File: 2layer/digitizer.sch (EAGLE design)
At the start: 56 parts, among them IC1 FT601QQFN76, X1 SMA-142-0711-881/886, X2 SMA-142-0711-881/886

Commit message: almost done allocating wires
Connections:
- net ADC_OEN: now also JP4.4
- net ADC_SLP: now also JP4.3
- net BE0: now also JP3.18; no longer JP4.24
- net BE1: now also JP3.17; no longer JP4.23
- net BE2: now also JP3.20; no longer JP4.26
- net BE3: now also JP3.19; no longer JP4.25
- net GND: now also JP3.11, JP3.12, JP3.31, JP3.32, JP3.39
- net GPIO0: now also JP3.29; no longer JP3.28
- net GPIO1: now also JP3.30; no longer JP3.27
- net OEN: now also JP3.28; no longer JP3.26
- net OVFL: now also JP3.16
- net RDN: now also JP3.27; no longer JP3.25
- net RXFN: now also JP3.24
- net SAMP0: now also JP3.3
- net SAMP1: now also JP3.6
- net SAMP2: now also JP3.5
- net SAMP3: now also JP3.8
- net SAMP4: now also JP3.7
- net SAMP5: now also JP3.10
- net SAMP6: now also JP3.9
- net SAMP7: now also JP3.13
- net SAMP8: now also JP3.14
- net SAMP9: now also JP3.15
- net SAMPCLK: now also JP3.4
- net SFT_RSTN: now also JP3.40
- net SFT_WKPN: now also JP3.38
- net SIWUN: now also JP3.25; no longer JP3.23
- net TXEN: now also JP3.23
- net WRN: now also JP3.26; no longer JP3.24

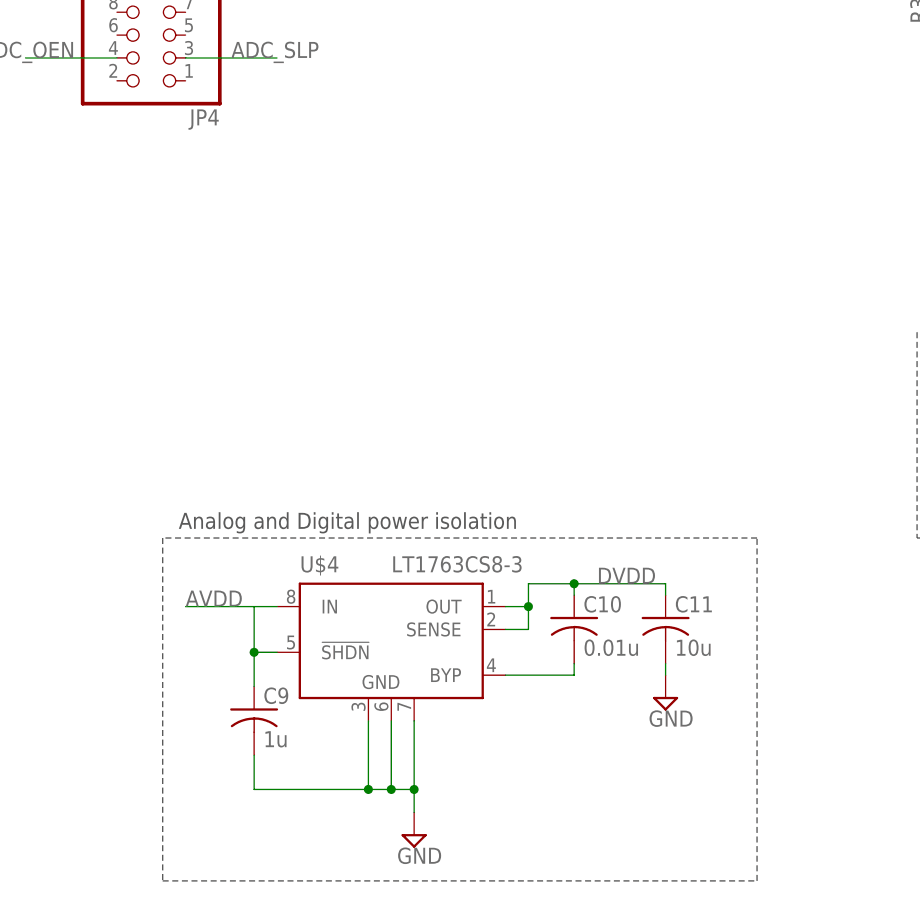
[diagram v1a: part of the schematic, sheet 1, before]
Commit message: added dual regulator solution for power isolation
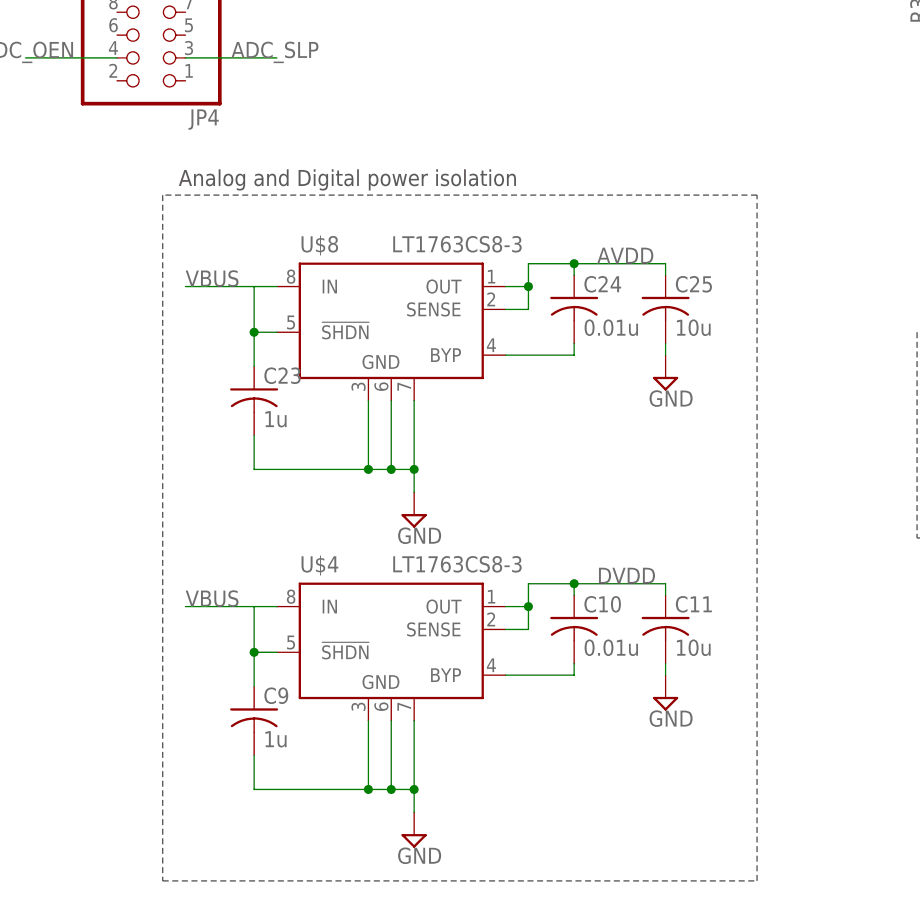
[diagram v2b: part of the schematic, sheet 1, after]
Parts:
- added C23: 1u, resistor:C-USC0402
- added C24: 0.01u, resistor:C-USC0402
- added C25: 10u, resistor:C-USC0402
- added U$8: LT1763CS8-3, linear-technology:LT1763CS8-3
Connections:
- new net N$16: C24.2, U$8.BYP
- net AVDD: now also C24.1, C25.1, U$8.OUT, U$8.SENSE; no longer C9.1, U$4.!SHDN, U$4.IN
- net GND: now also C23.2, C25.2, U$8.GND@1, U$8.GND@2, U$8.GND@3
- net VBUS: now also C23.1, C9.1, U$4.!SHDN, U$4.IN, U$8.!SHDN, U$8.IN
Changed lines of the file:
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@@
 <part name="SUPPLY37" library="supply2" deviceset="GND" device=""/>
 <part name="SUPPLY38" library="supply2" deviceset="GND" device=""/>
+<part name="U$8" library="linear-technology" deviceset="LT1763CS8" device="" technology="-3"/>
+<part name="C23" library="resistor" deviceset="C-US" device="C0402" value="1u"/>
+<part name="C24" library="resistor" deviceset="C-US" device="C0402" value="0.01u"/>
+<part name="C25" library="resistor" deviceset="C-US" device="C0402" value="10u"/>
+<part name="SUPPLY39" library="supply2" deviceset="GND" device=""/>
+<part name="SUPPLY40" library="supply2" deviceset="GND" device=""/>
 </parts>
 <sheets>
@@
 <wire x1="88.9" y1="-33.02" x2="35.56" y2="-33.02" width="0.1524" layer="97" style="longdash"/>
 <text x="37.338" y="-32.004" size="1.778" layer="97">Mixer impedance match and image filter</text>
-<wire x1="-48.26" y1="-55.88" x2="-48.26" y2="-93.98" width="0.1524" layer="97" style="longdash"/>
+<wire x1="-48.26" y1="-17.78" x2="-48.26" y2="-93.98" width="0.1524" layer="97" style="longdash"/>
 <wire x1="-48.26" y1="-93.98" x2="17.78" y2="-93.98" width="0.1524" layer="97" style="longdash"/>
-<wire x1="17.78" y1="-93.98" x2="17.78" y2="-55.88" width="0.1524" layer="97" style="longdash"/>
-<wire x1="17.78" y1="-55.88" x2="-48.26" y2="-55.88" width="0.1524" layer="97" style="longdash"/>
-<text x="-46.482" y="-54.864" size="1.778" layer="97">Analog and Digital power isolation</text>
+<wire x1="17.78" y1="-93.98" x2="17.78" y2="-17.78" width="0.1524" layer="97" style="longdash"/>
+<wire x1="17.78" y1="-17.78" x2="-48.26" y2="-17.78" width="0.1524" layer="97" style="longdash"/>
+<text x="-46.482" y="-16.764" size="1.778" layer="97">Analog and Digital power isolation</text>
 <text x="58.42" y="99.06" size="5.08" layer="97">Mixer</text>
 <text x="50.8" y="53.34" size="5.08" layer="97">ADC</text>
@@
 <instance part="SUPPLY37" gate="GND" x="-27.94" y="86.36" rot="R90"/>
 <instance part="SUPPLY38" gate="GND" x="-25.4" y="73.66" rot="R90"/>
+<instance part="U$8" gate="G$1" x="-22.86" y="-30.48"/>
+<instance part="C23" gate="G$1" x="-38.1" y="-39.37"/>
+<instance part="C24" gate="G$1" x="-2.54" y="-29.21"/>
+<instance part="C25" gate="G$1" x="7.62" y="-29.21"/>
+<instance part="SUPPLY39" gate="GND" x="-20.32" y="-53.34"/>
+<instance part="SUPPLY40" gate="GND" x="7.62" y="-38.1"/>
 </instances>
 <busses>
@@
 <pinref part="SUPPLY34" gate="GND" pin="GND"/>
 </segment>
+<segment>
+<pinref part="SUPPLY40" gate="GND" pin="GND"/>
+<pinref part="C25" gate="G$1" pin="2"/>
+<wire x1="7.62" y1="-35.56" x2="7.62" y2="-34.29" width="0.1524" layer="91"/>
+</segment>
+<segment>
+<pinref part="C23" gate="G$1" pin="2"/>
+<wire x1="-38.1" y1="-44.45" x2="-38.1" y2="-48.26" width="0.1524" layer="91"/>
+<wire x1="-38.1" y1="-48.26" x2="-25.4" y2="-48.26" width="0.1524" layer="91"/>
+<pinref part="U$8" gate="G$1" pin="GND@1"/>
+<wire x1="-25.4" y1="-48.26" x2="-25.4" y2="-40.64" width="0.1524" layer="91"/>
+<pinref part="U$8" gate="G$1" pin="GND@2"/>
+<wire x1="-25.4" y1="-48.26" x2="-22.86" y2="-48.26" width="0.1524" layer="91"/>
+<wire x1="-22.86" y1="-48.26" x2="-22.86" y2="-40.64" width="0.1524" layer="91"/>
+<junction x="-25.4" y="-48.26"/>
+<pinref part="U$8" gate="G$1" pin="GND@3"/>
+<wire x1="-22.86" y1="-48.26" x2="-20.32" y2="-48.26" width="0.1524" layer="91"/>
+<wire x1="-20.32" y1="-48.26" x2="-20.32" y2="-40.64" width="0.1524" layer="91"/>
+<junction x="-22.86" y="-48.26"/>
+<pinref part="SUPPLY39" gate="GND" pin="GND"/>
+<wire x1="-20.32" y1="-48.26" x2="-20.32" y2="-50.8" width="0.1524" layer="91"/>
+<junction x="-20.32" y="-48.26"/>
+</segment>
 </net>
 <net name="AVDD" class="0">
@@
 </segment>
 <segment>
-<pinref part="U$4" gate="G$1" pin="IN"/>
-<wire x1="-35.56" y1="-63.5" x2="-38.1" y2="-63.5" width="0.1524" layer="91"/>
-<pinref part="C9" gate="G$1" pin="1"/>
-<wire x1="-45.72" y1="-63.5" x2="-38.1" y2="-63.5" width="0.1524" layer="91"/>
-<wire x1="-38.1" y1="-63.5" x2="-38.1" y2="-68.58" width="0.1524" layer="91"/>
-<pinref part="U$4" gate="G$1" pin="!SHDN"/>
-<wire x1="-38.1" y1="-68.58" x2="-38.1" y2="-72.39" width="0.1524" layer="91"/>
-<wire x1="-35.56" y1="-68.58" x2="-38.1" y2="-68.58" width="0.1524" layer="91"/>
-<junction x="-38.1" y="-68.58"/>
-<label x="-45.72" y="-63.5" size="1.778" layer="95"/>
-</segment>
-<segment>
 <wire x1="-76.2" y1="-73.66" x2="-81.28" y2="-73.66" width="0.1524" layer="91"/>
 <wire x1="-81.28" y1="-73.66" x2="-81.28" y2="-71.12" width="0.1524" layer="91"/>
@@
 <wire x1="-104.14" y1="-73.66" x2="-104.14" y2="-71.12" width="0.1524" layer="91"/>
 <pinref part="R12" gate="G$1" pin="1"/>
+</segment>
+<segment>
+<pinref part="U$8" gate="G$1" pin="SENSE"/>
+<wire x1="-10.16" y1="-30.48" x2="-7.62" y2="-30.48" width="0.1524" layer="91"/>
+<wire x1="-7.62" y1="-30.48" x2="-7.62" y2="-27.94" width="0.1524" layer="91"/>
+<pinref part="U$8" gate="G$1" pin="OUT"/>
+<wire x1="-7.62" y1="-27.94" x2="-10.16" y2="-27.94" width="0.1524" layer="91"/>
+<wire x1="-7.62" y1="-27.94" x2="-7.62" y2="-25.4" width="0.1524" layer="91"/>
+<junction x="-7.62" y="-27.94"/>
+<pinref part="C25" gate="G$1" pin="1"/>
+<wire x1="-7.62" y1="-25.4" x2="-2.54" y2="-25.4" width="0.1524" layer="91"/>
+<wire x1="-2.54" y1="-25.4" x2="7.62" y2="-25.4" width="0.1524" layer="91"/>
+<wire x1="7.62" y1="-25.4" x2="7.62" y2="-26.67" width="0.1524" layer="91"/>
+<pinref part="C24" gate="G$1" pin="1"/>
+<wire x1="-2.54" y1="-26.67" x2="-2.54" y2="-25.4" width="0.1524" layer="91"/>
+<junction x="-2.54" y="-25.4"/>
+<label x="0" y="-25.4" size="1.778" layer="95"/>
 </segment>
 </net>
@@
 </segment>
 </net>
+<net name="N$16" class="0">
+<segment>
+<pinref part="U$8" gate="G$1" pin="BYP"/>
+<pinref part="C24" gate="G$1" pin="2"/>
+<wire x1="-10.16" y1="-35.56" x2="-2.54" y2="-35.56" width="0.1524" layer="91"/>
+<wire x1="-2.54" y1="-35.56" x2="-2.54" y2="-34.29" width="0.1524" layer="91"/>
+</segment>
+</net>
+<net name="VBUS" class="0">
+<segment>
+<pinref part="U$8" gate="G$1" pin="IN"/>
+<wire x1="-35.56" y1="-27.94" x2="-38.1" y2="-27.94" width="0.1524" layer="91"/>
+<pinref part="C23" gate="G$1" pin="1"/>
+<wire x1="-45.72" y1="-27.94" x2="-38.1" y2="-27.94" width="0.1524" layer="91"/>
+<wire x1="-38.1" y1="-27.94" x2="-38.1" y2="-33.02" width="0.1524" layer="91"/>
+<pinref part="U$8" gate="G$1" pin="!SHDN"/>
+<wire x1="-38.1" y1="-33.02" x2="-38.1" y2="-36.83" width="0.1524" layer="91"/>
+<wire x1="-35.56" y1="-33.02" x2="-38.1" y2="-33.02" width="0.1524" layer="91"/>
+<junction x="-38.1" y="-33.02"/>
+<label x="-45.72" y="-27.94" size="1.778" layer="95"/>
+</segment>
+<segment>
+<pinref part="U$4" gate="G$1" pin="IN"/>
+<wire x1="-35.56" y1="-63.5" x2="-38.1" y2="-63.5" width="0.1524" layer="91"/>
+<pinref part="C9" gate="G$1" pin="1"/>
+<wire x1="-45.72" y1="-63.5" x2="-38.1" y2="-63.5" width="0.1524" layer="91"/>
+<wire x1="-38.1" y1="-63.5" x2="-38.1" y2="-68.58" width="0.1524" layer="91"/>
+<pinref part="U$4" gate="G$1" pin="!SHDN"/>
+<wire x1="-38.1" y1="-68.58" x2="-38.1" y2="-72.39" width="0.1524" layer="91"/>
+<wire x1="-35.56" y1="-68.58" x2="-38.1" y2="-68.58" width="0.1524" layer="91"/>
+<junction x="-38.1" y="-68.58"/>
+<label x="-45.72" y="-63.5" size="1.778" layer="95"/>
+</segment>
+</net>

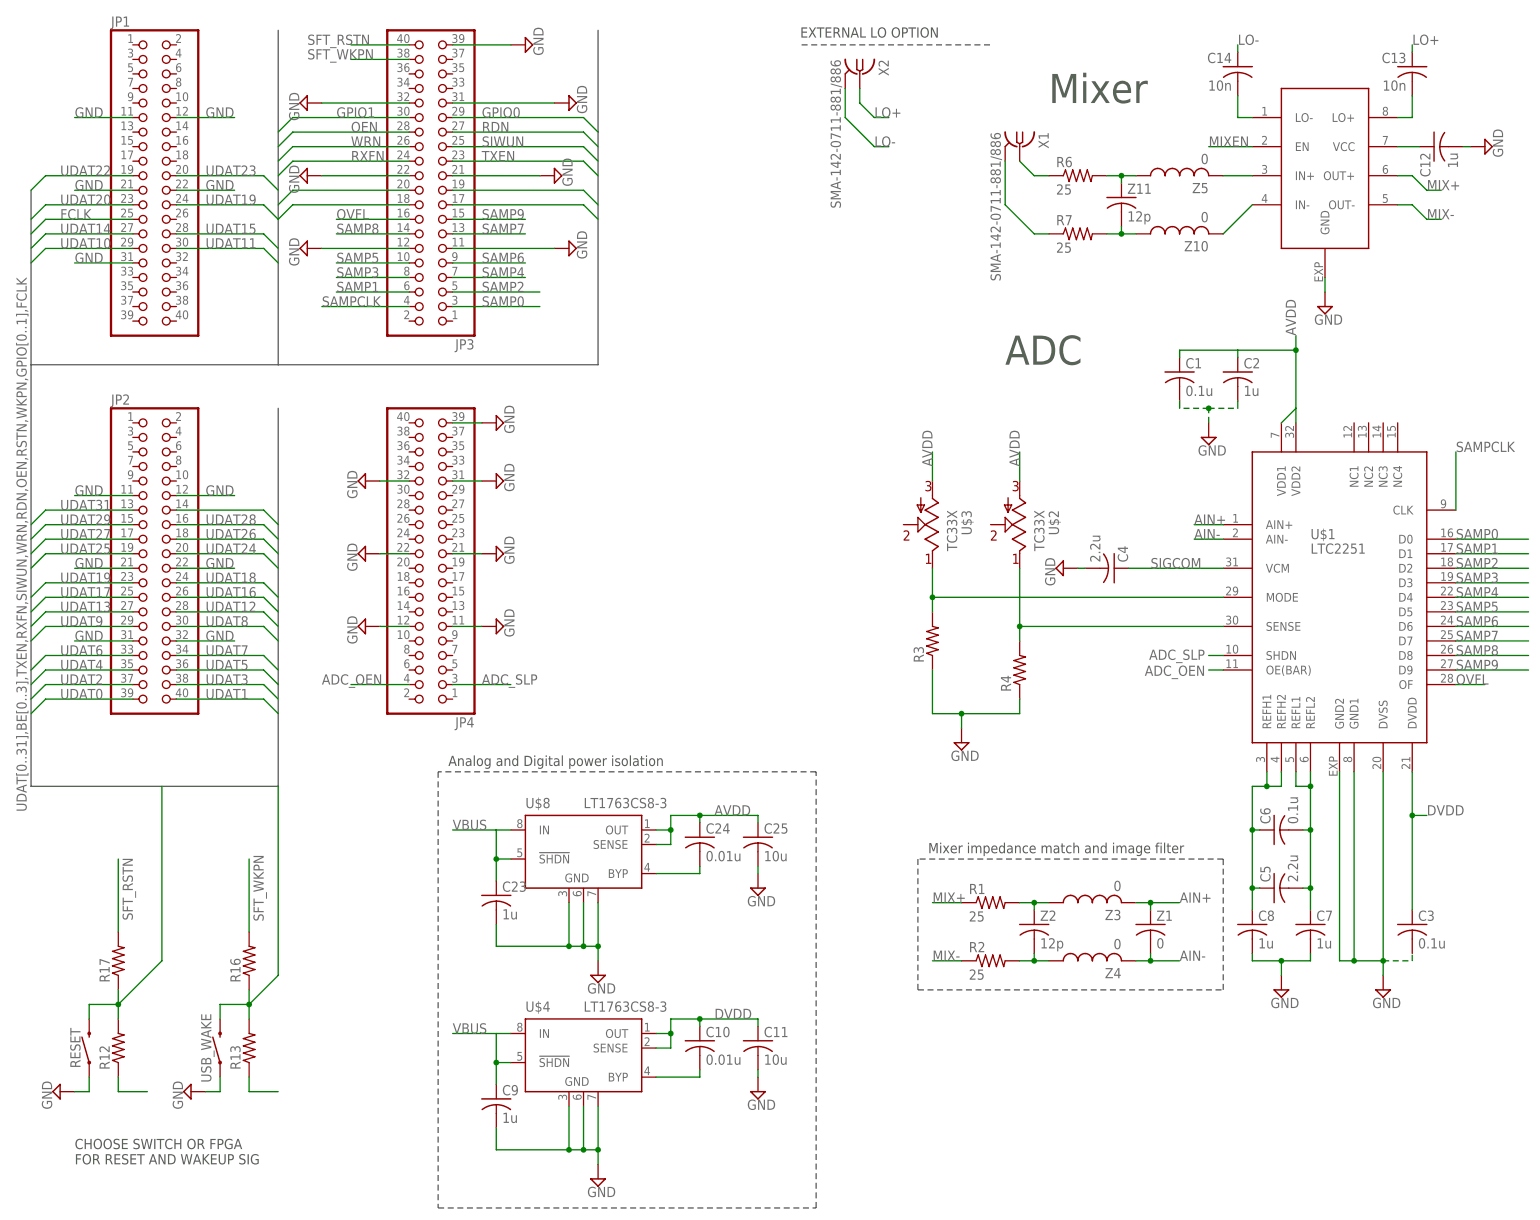
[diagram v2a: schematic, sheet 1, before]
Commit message: added pours
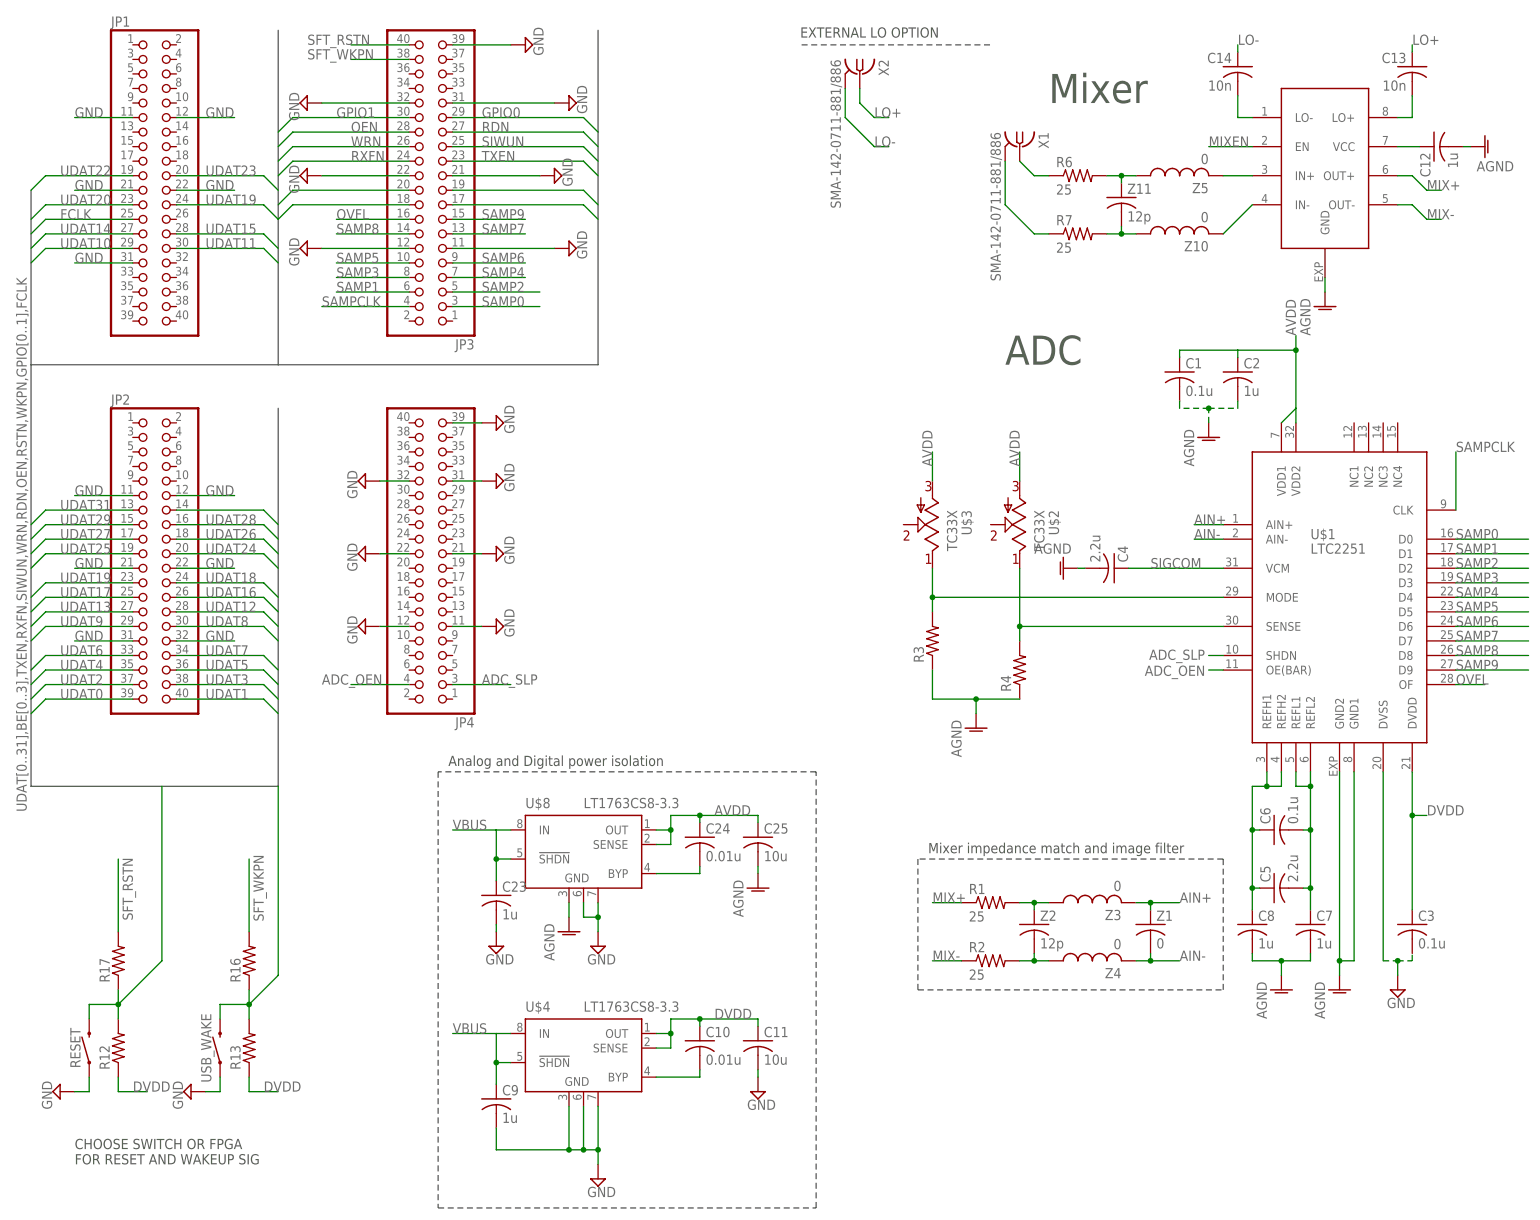
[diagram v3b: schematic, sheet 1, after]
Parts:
- U$4, U$8: value LT1763CS8-3 -> LT1763CS8-3.3; device linear-technology:LT1763CS8-3 -> linear-technology:LT1763CS8-3.3
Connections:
- new net AGND: C1.2, C12.2, C2.2, C25.2, C4.2, C7.2, C8.2, R3.1, R4.1, U$1.GND1, U$1.GND2, U$5.GND, U$8.GND@1
- net AVDD: no longer R12.1, R13.1
- net DVDD: now also R12.1, R13.1
- net GND: no longer C1.2, C12.2, C2.2, C25.2, C4.2, C7.2, C8.2, R3.1, R4.1, U$1.GND1, U$1.GND2, U$5.GND, U$8.GND@1
